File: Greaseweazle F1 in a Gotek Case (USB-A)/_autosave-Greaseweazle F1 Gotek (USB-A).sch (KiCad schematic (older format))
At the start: 18 parts, among them CN1 FLOPPY, J1 USB A, J2 Floppy Power, J3 Programming Port, SW1 SW_Push, U1 Blue Pill

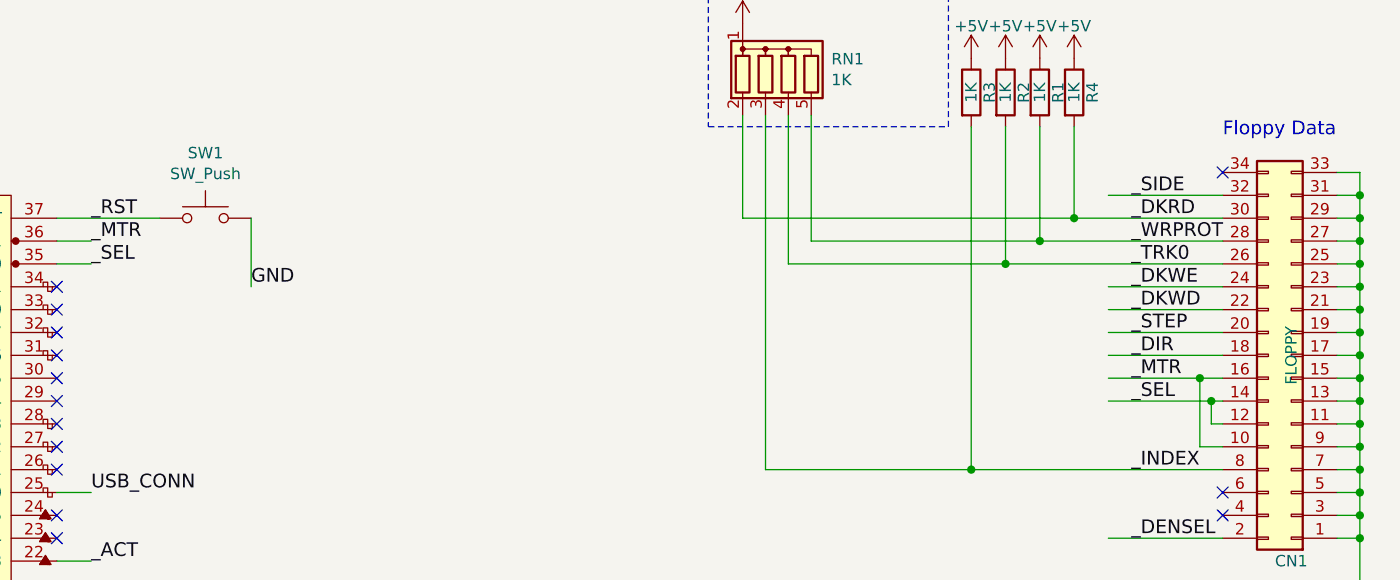
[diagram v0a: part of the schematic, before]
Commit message: More improvements and corrections
* moved USB header
* Reset switch
* Corrected SWD labelling
* Added DPDT On-On-On toggle switch silk screen
* Cleaned up LED silk screen
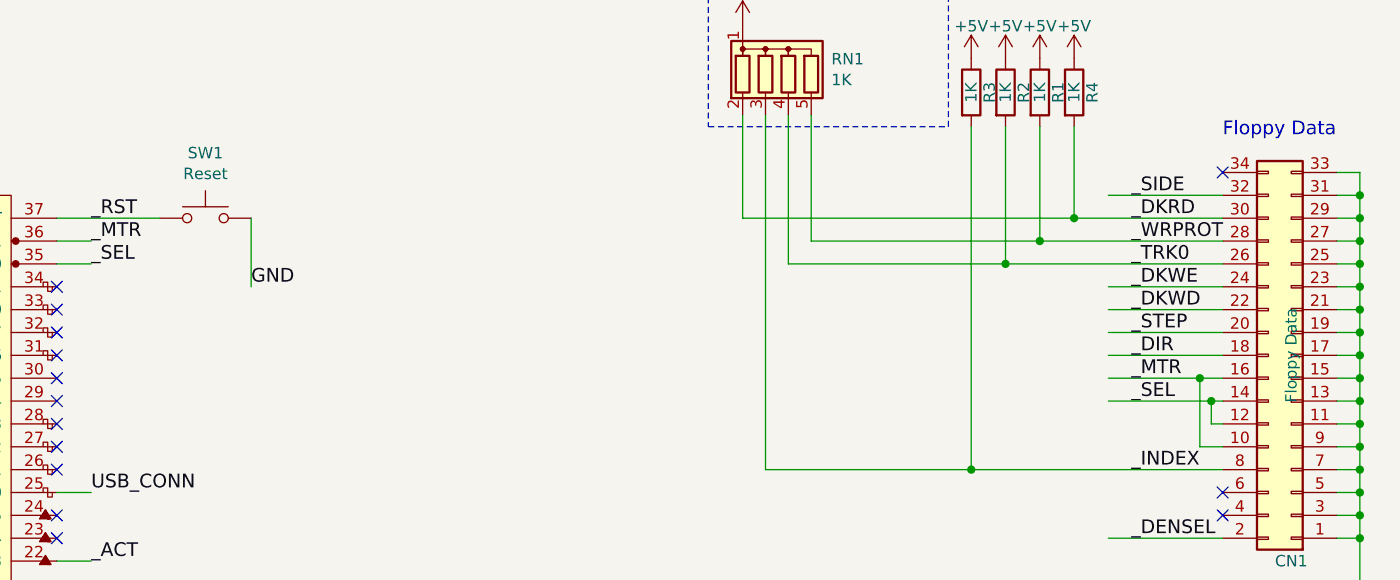
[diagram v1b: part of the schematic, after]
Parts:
- CN1: value FLOPPY -> Floppy Data
- SW1: value SW_Push -> Reset
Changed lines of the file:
@@
 P 10650 5250
 F 0 "CN1" H 10650 6150 50  0000 C CNN
-F 1 "FLOPPY" V 10650 5250 50  0000 C CNN
+F 1 "Floppy Data" V 10650 5250 50  0000 C CNN
 F 2 "Connector_PinHeader_2.54mm:PinHeader_2x17_P2.54mm_Vertical" H 10650 4150 60  0001 C CNN
 F 3 "" H 10650 4150 60  0000 C CNN
@@
 P 5900 4650
 F 0 "SW1" H 5900 4935 50  0000 C CNN
-F 1 "SW_Push" H 5900 4844 50  0000 C CNN
+F 1 "Reset" H 5900 4844 50  0000 C CNN
 F 2 "OpenFlops:PUSH_BUTTON_RIGHT_ANGLE" H 5900 4850 50  0001 C CNN
 F 3 "~" H 5900 4850 50  0001 C CNN
